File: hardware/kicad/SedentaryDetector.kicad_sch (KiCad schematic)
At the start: 2 parts, among them J1 ESP32_2x15, J2 MPU6050_1x8

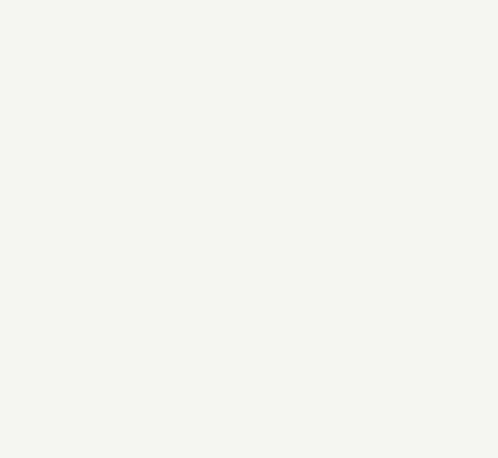
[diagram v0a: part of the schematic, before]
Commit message: docs(sch): add J3 POWER_2P power connector
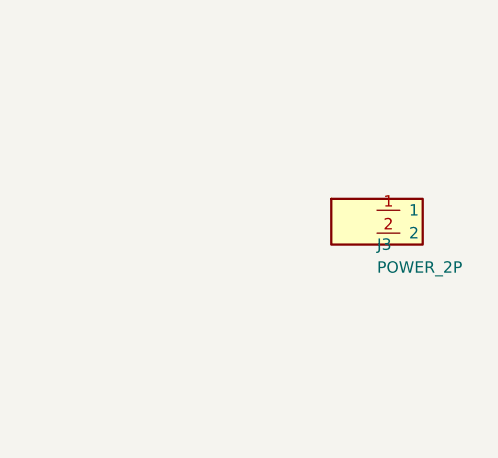
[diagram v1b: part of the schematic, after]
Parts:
- added J3: POWER_2P, symbol Conn_01x02
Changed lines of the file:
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@@
 		)
 	)
-	(sheet_instances
+	(symbol (lib_id "Conn_01x02") (at 300 100 0) (unit 1) (in_bom yes) (on_board yes)
+		(property "Reference" "J3" (at 300 102.54 0) (effects (font (size 1.27 1.27)) (justify left)))
+		(property "Value" "POWER_2P" (at 300 105.08 0) (effects (font (size 1.27 1.27)) (justify left)))
+		(property "Footprint" "" (at 300 97.5 0) (effects (font (size 1.27 1.27)) (hide yes)))
+		(property "Datasheet" "~" (at 300 100 0) (effects (font (size 1.27 1.27)) (hide yes)))
+		(pin "1")
+		(pin "2")
+	)
+(sheet_instances
 		(path "/"
 			(page "1")

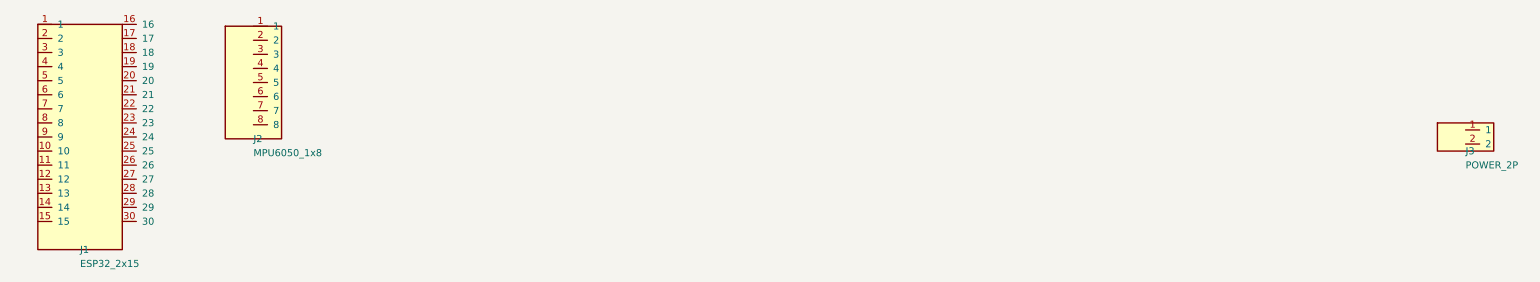
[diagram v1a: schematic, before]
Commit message: feat(hardware): add board outline through MH
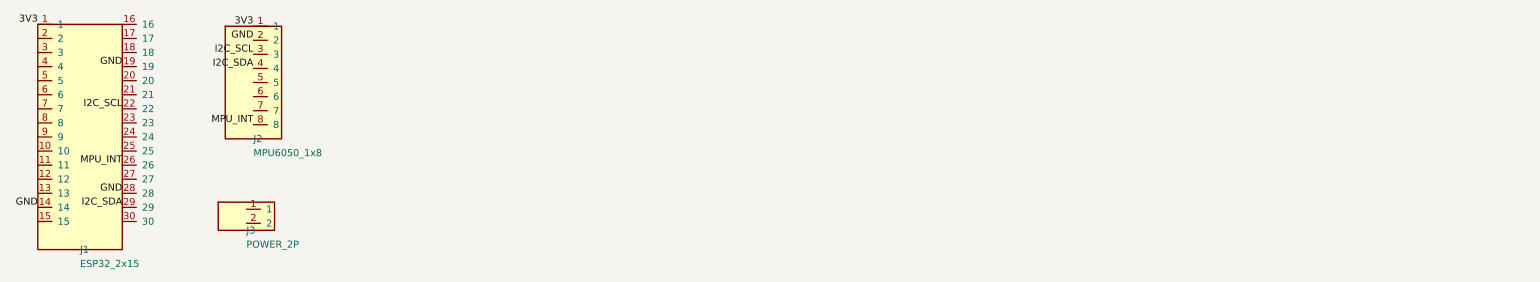
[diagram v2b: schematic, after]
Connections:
- net 3V3: now reaches J2.1
- net 3V3: now also J1.1
- net GND: now reaches J2.2
- net GND: now also J1.14, J1.19, J1.28
- net I2C_SCL: now reaches J2.3
- net I2C_SCL: now also J1.22
- net I2C_SDA: now reaches J2.4
- net I2C_SDA: now also J1.29
- net MPU_INT: now reaches J2.8
- net MPU_INT: now also J1.26
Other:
- moved on the sheet: J3
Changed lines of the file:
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@@
 		(rev "0.2")
+	)
+	(label "3V3"
+		(at 42.38 79.68 180)
+		(effects
+			(font
+				(size 1.27 1.27)
+			)
+			(justify right bottom)
+		)
+	)
+	(label "MPU_INT"
+		(at 57.62 105.08 180)
+		(effects
+			(font
+				(size 1.27 1.27)
+			)
+			(justify right bottom)
+		)
+	)
+	(label "GND"
+		(at 81.28 82.55 180)
+		(effects
+			(font
+				(size 1.27 1.27)
+			)
+			(justify right bottom)
+		)
+	)
+	(label "I2C_SCL"
+		(at 81.28 85.09 180)
+		(effects
+			(font
+				(size 1.27 1.27)
+			)
+			(justify right bottom)
+		)
+	)
+	(label "I2C_SDA"
+		(at 81.28 87.63 180)
+		(effects
+			(font
+				(size 1.27 1.27)
+			)
+			(justify right bottom)
+		)
+	)
+	(label "I2C_SDA"
+		(at 57.62 112.7 180)
+		(effects
+			(font
+				(size 1.27 1.27)
+			)
+			(justify right bottom)
+		)
+	)
+	(label "3V3"
+		(at 81.28 80.01 180)
+		(effects
+			(font
+				(size 1.27 1.27)
+			)
+			(justify right bottom)
+		)
+	)
+	(label "GND"
+		(at 57.62 87.3 180)
+		(effects
+			(font
+				(size 1.27 1.27)
+			)
+			(justify right bottom)
+		)
+	)
+	(label "MPU_INT"
+		(at 81.28 97.79 180)
+		(effects
+			(font
+				(size 1.27 1.27)
+			)
+			(justify right bottom)
+		)
+	)
+	(label "GND"
+		(at 57.62 110.16 180)
+		(effects
+			(font
+				(size 1.27 1.27)
+			)
+			(justify right bottom)
+		)
+	)
+	(label "GND"
+		(at 42.38 112.7 180)
+		(effects
+			(font
+				(size 1.27 1.27)
+			)
+			(justify right bottom)
+		)
+	)
+	(label "I2C_SCL"
+		(at 57.62 94.92 180)
+		(effects
+			(font
+				(size 1.27 1.27)
+			)
+			(justify right bottom)
+		)
+	)
+	(symbol
+		(lib_id "Conn_01x02")
+		(at 80.01 114.3 0)
+		(unit 1)
+		(body_style 1)
+		(exclude_from_sim no)
+		(in_bom yes)
+		(on_board yes)
+		(in_pos_files yes)
+		(dnp no)
+		(property "Reference" "J3"
+			(at 80.01 116.84 0)
+			(show_name no)
+			(do_not_autoplace no)
+			(effects
+				(font
+					(size 1.27 1.27)
+				)
+				(justify left)
+			)
+		)
+		(property "Value" "POWER_2P"
+			(at 80.01 119.38 0)
+			(show_name no)
+			(do_not_autoplace no)
+			(effects
+				(font
+					(size 1.27 1.27)
+				)
+				(justify left)
+			)
+		)
+		(property "Footprint" ""
+			(at 80.01 111.8 0)
+			(hide yes)
+			(show_name no)
+			(do_not_autoplace no)
+			(effects
+				(font
+					(size 1.27 1.27)
+				)
+			)
+		)
+		(property "Datasheet" "~"
+			(at 80.01 114.3 0)
+			(hide yes)
+			(show_name no)
+			(do_not_autoplace no)
+			(effects
+				(font
+					(size 1.27 1.27)
+				)
+			)
+		)
+		(property "Description" ""
+			(at 80.01 114.3 0)
+			(show_name no)
+			(do_not_autoplace no)
+			(effects
+				(font
+					(size 1.27 1.27)
+				)
+			)
+		)
+		(pin "1"
+		)
+		(pin "2"
+		)
+		(instances
+			(project "SedentaryDetector"
+				(path "/c9bb8533-5510-495a-86a1-47335bb4bfe4"
+					(reference "J3")
+					(unit 1)
+				)
+			)
+		)
 	)
 	(symbol
@@
 		)
 	)
-	(symbol (lib_id "Conn_01x02") (at 300 100 0) (unit 1) (in_bom yes) (on_board yes)
-		(property "Reference" "J3" (at 300 102.54 0) (effects (font (size 1.27 1.27)) (justify left)))
-		(property "Value" "POWER_2P" (at 300 105.08 0) (effects (font (size 1.27 1.27)) (justify left)))
-		(property "Footprint" "" (at 300 97.5 0) (effects (font (size 1.27 1.27)) (hide yes)))
-		(property "Datasheet" "~" (at 300 100 0) (effects (font (size 1.27 1.27)) (hide yes)))
-		(pin "1")
-		(pin "2")
-	)
-(sheet_instances
+	(sheet_instances
 		(path "/"
 			(page "1")
